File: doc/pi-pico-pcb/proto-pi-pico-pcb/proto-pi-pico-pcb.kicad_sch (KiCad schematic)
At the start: 13 parts

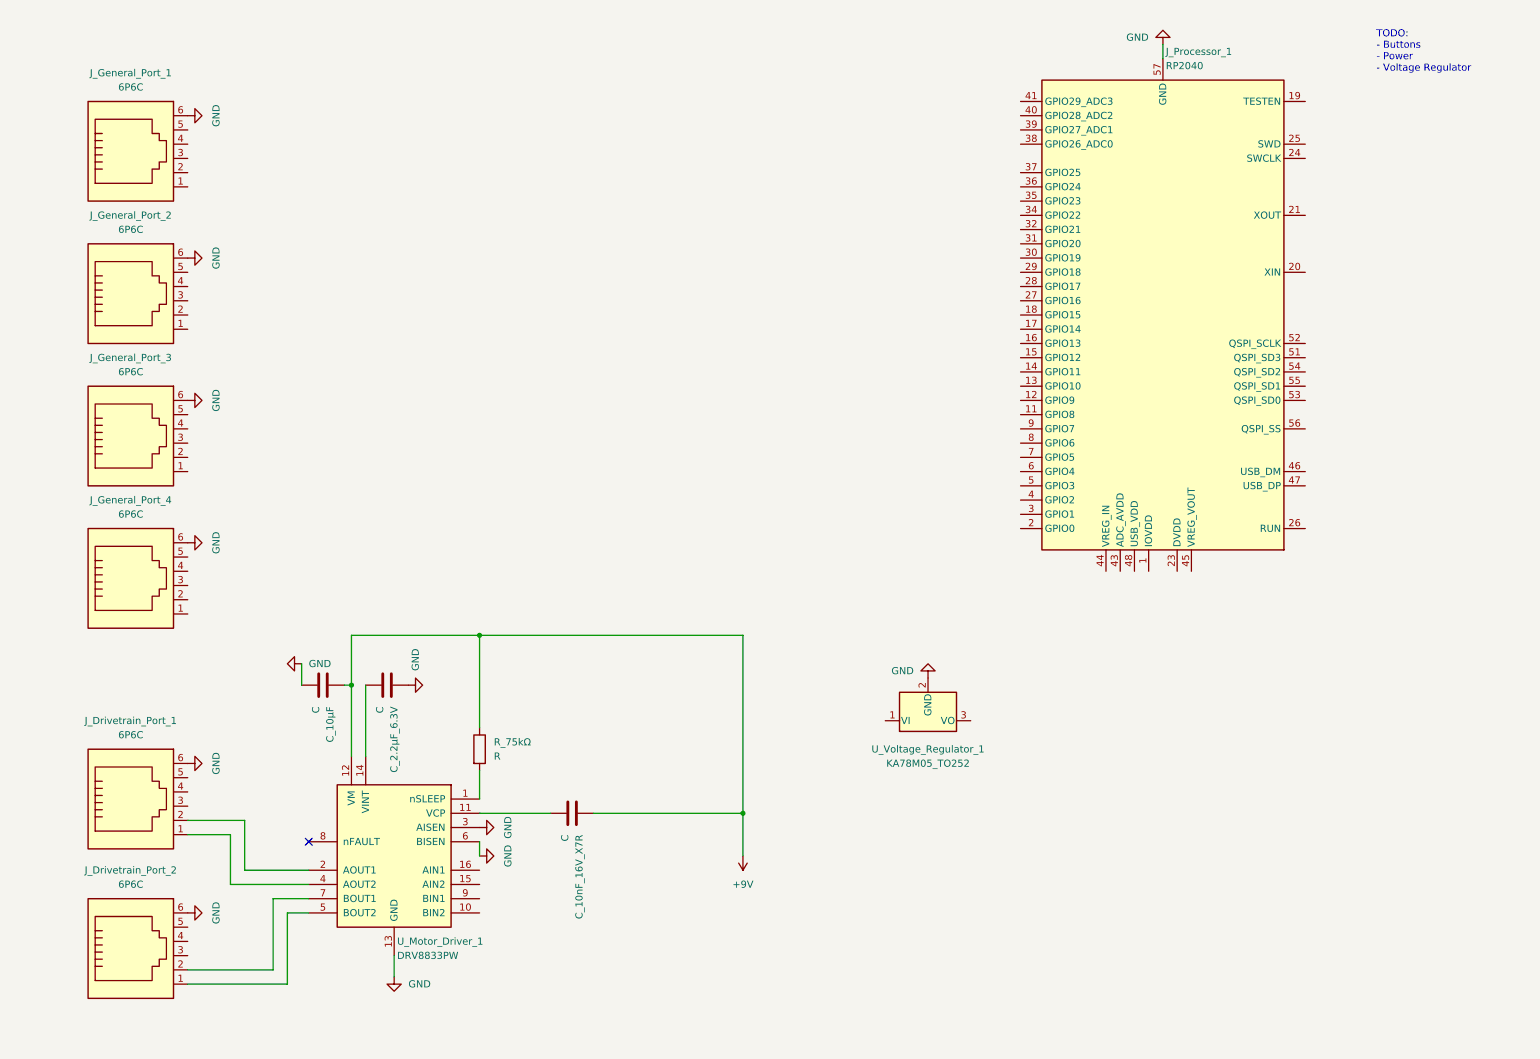
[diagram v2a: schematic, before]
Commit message: wired up external ports to bus
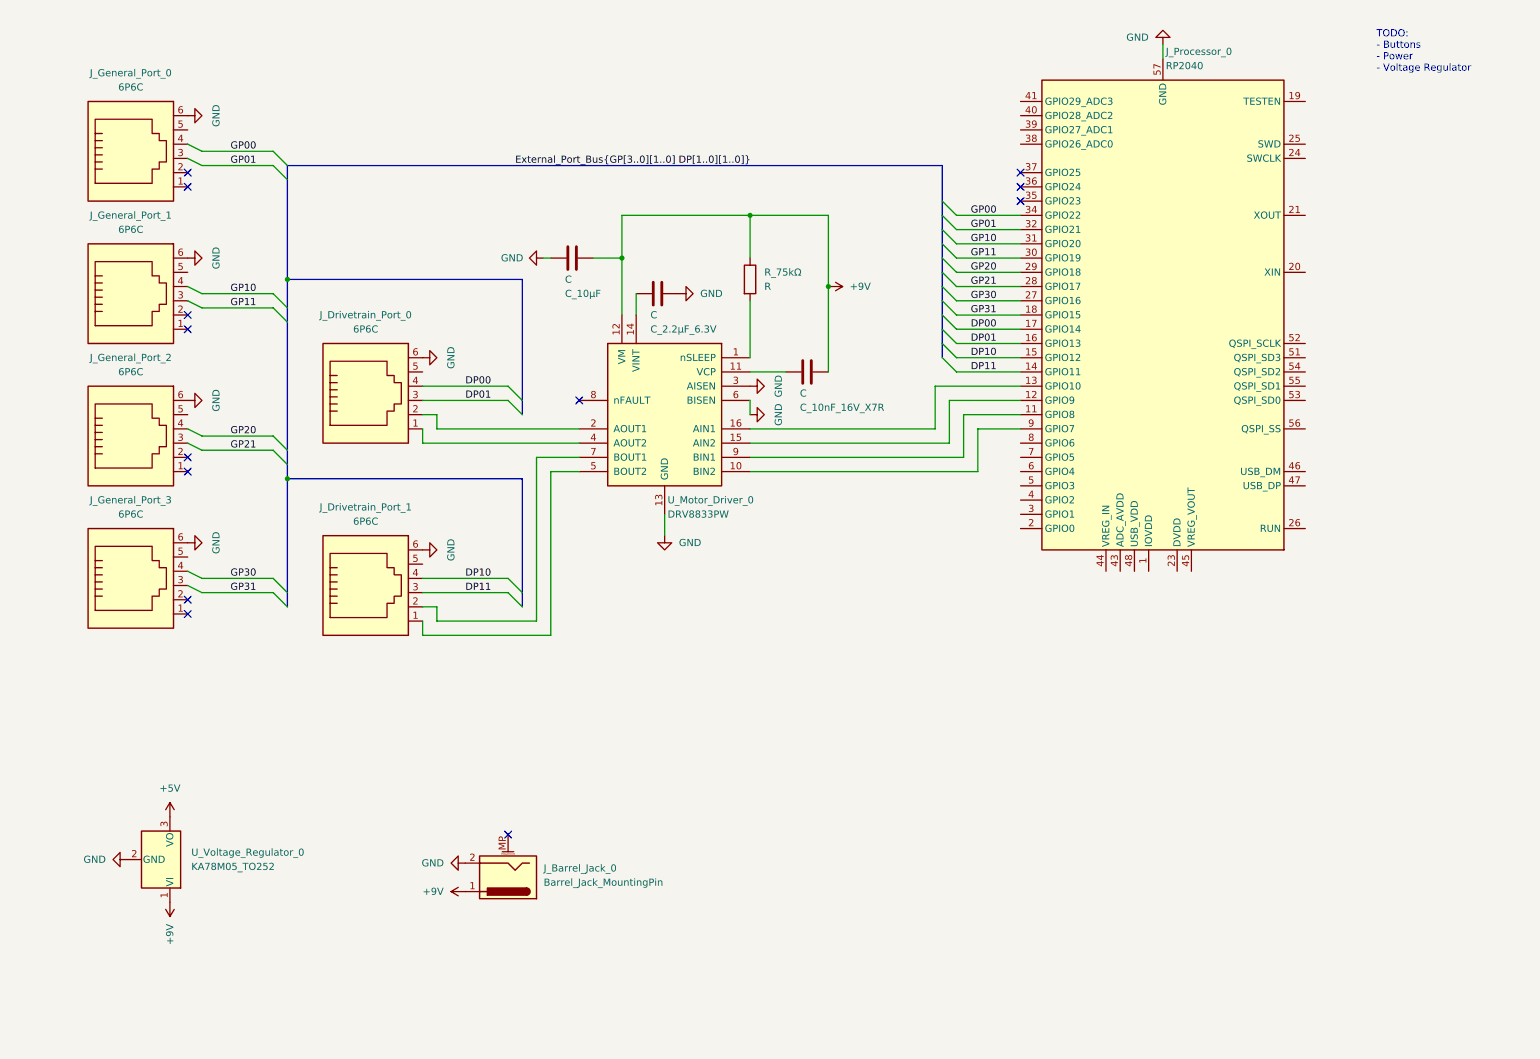
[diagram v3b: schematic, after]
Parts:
- added J_Barrel_Jack_0: Barrel_Jack_MountingPin, symbol Connector:Barrel_Jack_MountingPin
- renumbered J_Drivetrain_Port_1 to J_Drivetrain_Port_0, J_Drivetrain_Port_2 to J_Drivetrain_Port_1, J_General_Port_1 to J_General_Port_0, J_General_Port_2 to J_General_Port_1, J_General_Port_3 to J_General_Port_2, J_General_Port_4 to J_General_Port_3, J_Processor_1 to J_Processor_0, U_Motor_Driver_1 to U_Motor_Driver_0, U_Voltage_Regulator_1 to U_Voltage_Regulator_0
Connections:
- net +9V: now also U_Voltage_Regulator_0.1 (VI), J_Barrel_Jack_0.1
- net GND: now also J_Barrel_Jack_0.2
- net GP01: now reaches J_General_Port_0.3
- net GP01: now also J_Processor_0.32 (GPIO21)
- net GP00: now reaches J_General_Port_0.4
- net GP00: now also J_Processor_0.34 (GPIO22)
- net DP01: now reaches J_Drivetrain_Port_0.3
- net DP01: now also J_Processor_0.16 (GPIO13)
- net DP00: now reaches J_Drivetrain_Port_0.4
- net DP00: now also J_Processor_0.17 (GPIO14)
- net at J_Processor_0.11 (GPIO8): now also U_Motor_Driver_0.9 (BIN1)
- net at J_Processor_0.12 (GPIO9): now also U_Motor_Driver_0.15 (AIN2)
- net at J_Processor_0.13 (GPIO10): now also U_Motor_Driver_0.16 (AIN1)
- net DP11: now reaches J_Processor_0.14 (GPIO11)
- net DP11: now also J_Drivetrain_Port_1.3
- net DP10: now reaches J_Processor_0.15 (GPIO12)
- net DP10: now also J_Drivetrain_Port_1.4
- net GP31: now reaches J_Processor_0.18 (GPIO15)
- net GP31: now also J_General_Port_3.3
- net GP30: now reaches J_Processor_0.27 (GPIO16)
- net GP30: now also J_General_Port_3.4
- net GP21: now reaches J_Processor_0.28 (GPIO17)
- net GP21: now also J_General_Port_2.3
- net GP20: now reaches J_Processor_0.29 (GPIO18)
- net GP20: now also J_General_Port_2.4
- net GP11: now reaches J_Processor_0.30 (GPIO19)
- net GP11: now also J_General_Port_1.3
- net GP10: now reaches J_Processor_0.31 (GPIO20)
- net GP10: now also J_General_Port_1.4
- net at J_Processor_0.9 (GPIO7): now also U_Motor_Driver_0.10 (BIN2)
- net +5V: now reaches U_Voltage_Regulator_0.3 (VO)
- no-connect marks 1 -> 13
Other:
- moved on the sheet: C_10nF_16V_X7R, C_10μF, C_2.2μF_6.3V, J_Drivetrain_Port_0, J_Drivetrain_Port_1, R_75kΩ, U_Motor_Driver_0, U_Voltage_Regulator_0

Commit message: added general barrel jack
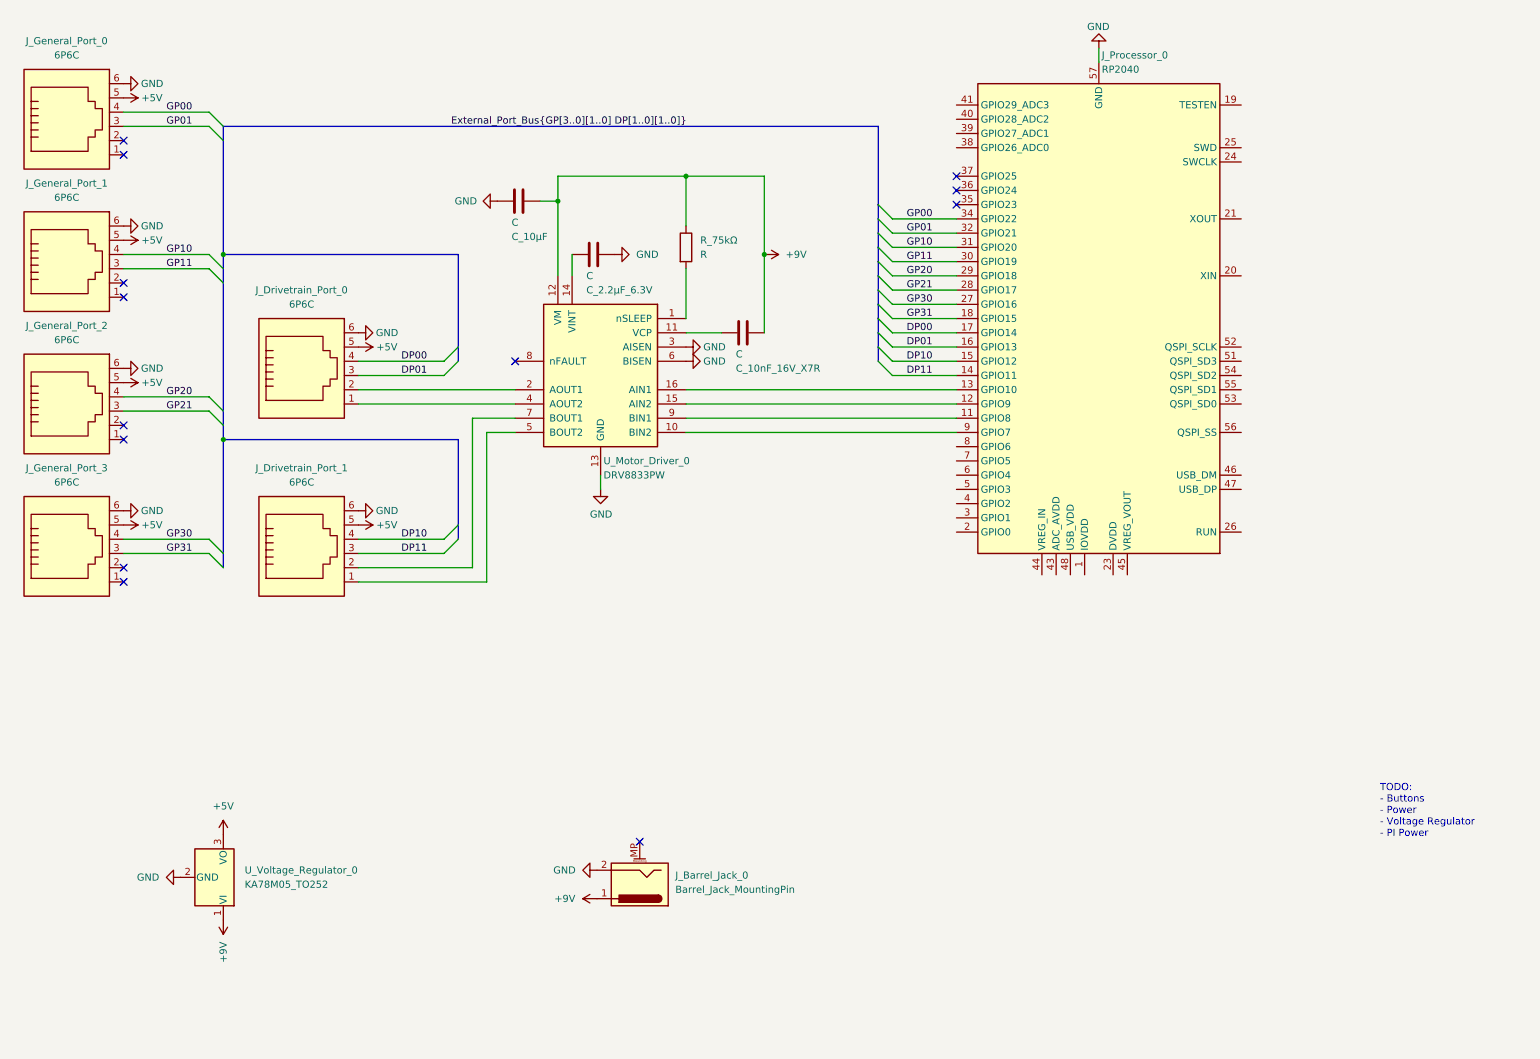
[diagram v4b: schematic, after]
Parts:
- J_Barrel_Jack_0: footprint (none) -> Connector_BarrelJack:BarrelJack_Horizontal
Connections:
- net +5V: now also J_Drivetrain_Port_0.5, J_Drivetrain_Port_1.5, J_General_Port_0.5, J_General_Port_1.5, J_General_Port_2.5, J_General_Port_3.5
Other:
- note added: "TODO: - Buttons - Power - Voltage Regulator - PI Power"
- note removed: "TODO: - Buttons - Power - Voltage Regulator"
- moved on the sheet: C_10nF_16V_X7R, C_10μF, C_2.2μF_6.3V, J_Barrel_Jack_0, J_Drivetrain_Port_0, J_Drivetrain_Port_1, J_General_Port_0, J_General_Port_1, J_General_Port_2, J_General_Port_3, J_Processor_0, R_75kΩ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

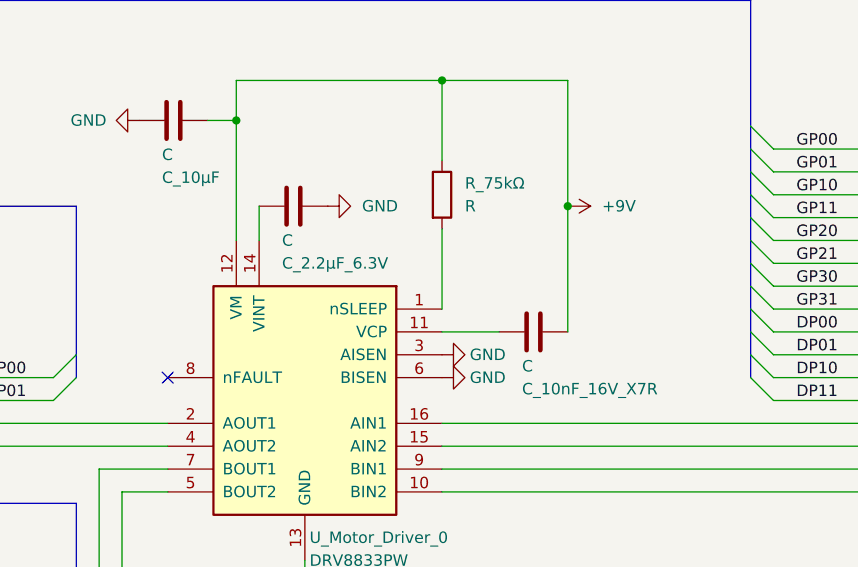
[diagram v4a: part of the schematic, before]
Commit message: gave general parts temporary footprints
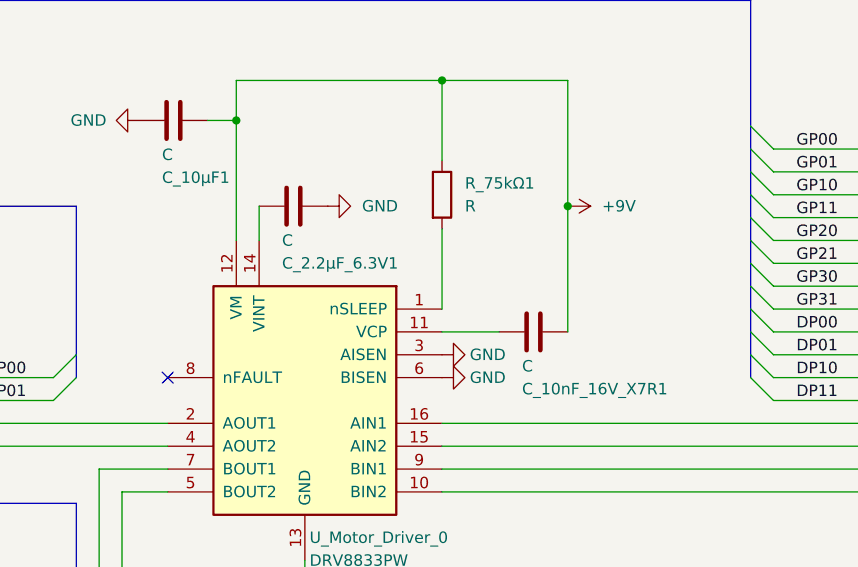
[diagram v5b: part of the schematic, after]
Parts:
- C_10nF_16V_X7R1: renamed from C_10nF_16V_X7R; footprint (none) -> Capacitor_SMD:CP_Elec_3x5.3
- C_10μF1: renamed from C_10μF; footprint (none) -> Capacitor_SMD:CP_Elec_3x5.3
- C_2.2μF_6.3V1: renamed from C_2.2μF_6.3V; footprint (none) -> Capacitor_SMD:CP_Elec_3x5.3
- J_Barrel_Jack_0: footprint Connector_BarrelJack:BarrelJack_Horizontal -> Connector_BarrelJack:BarrelJack_CUI_PJ-063AH_Horizontal
- J_Drivetrain_Port_0, J_Drivetrain_Port_1, J_General_Port_0, J_General_Port_1, J_General_Port_2, J_General_Port_3: footprint (none) -> Connector_RJ:RJ12_Amphenol_54601
- R_75kΩ1: renamed from R_75kΩ; footprint (none) -> Resistor_SMD:R_0201_0603Metric

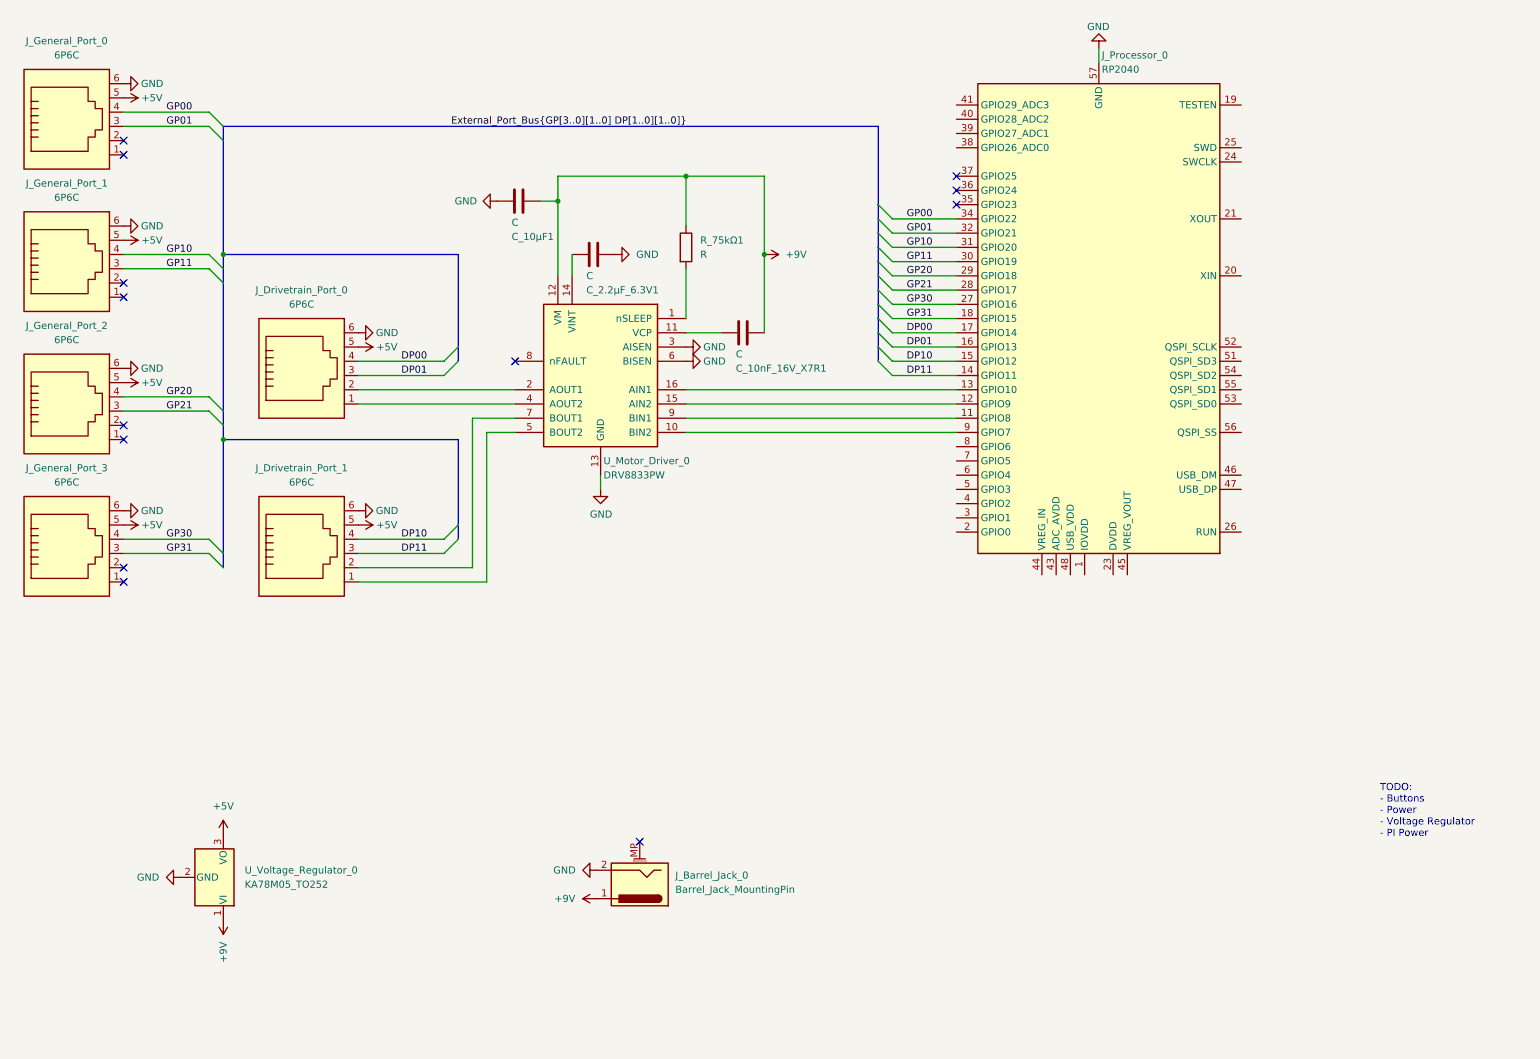
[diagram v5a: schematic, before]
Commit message: removed dead pins on rp2040
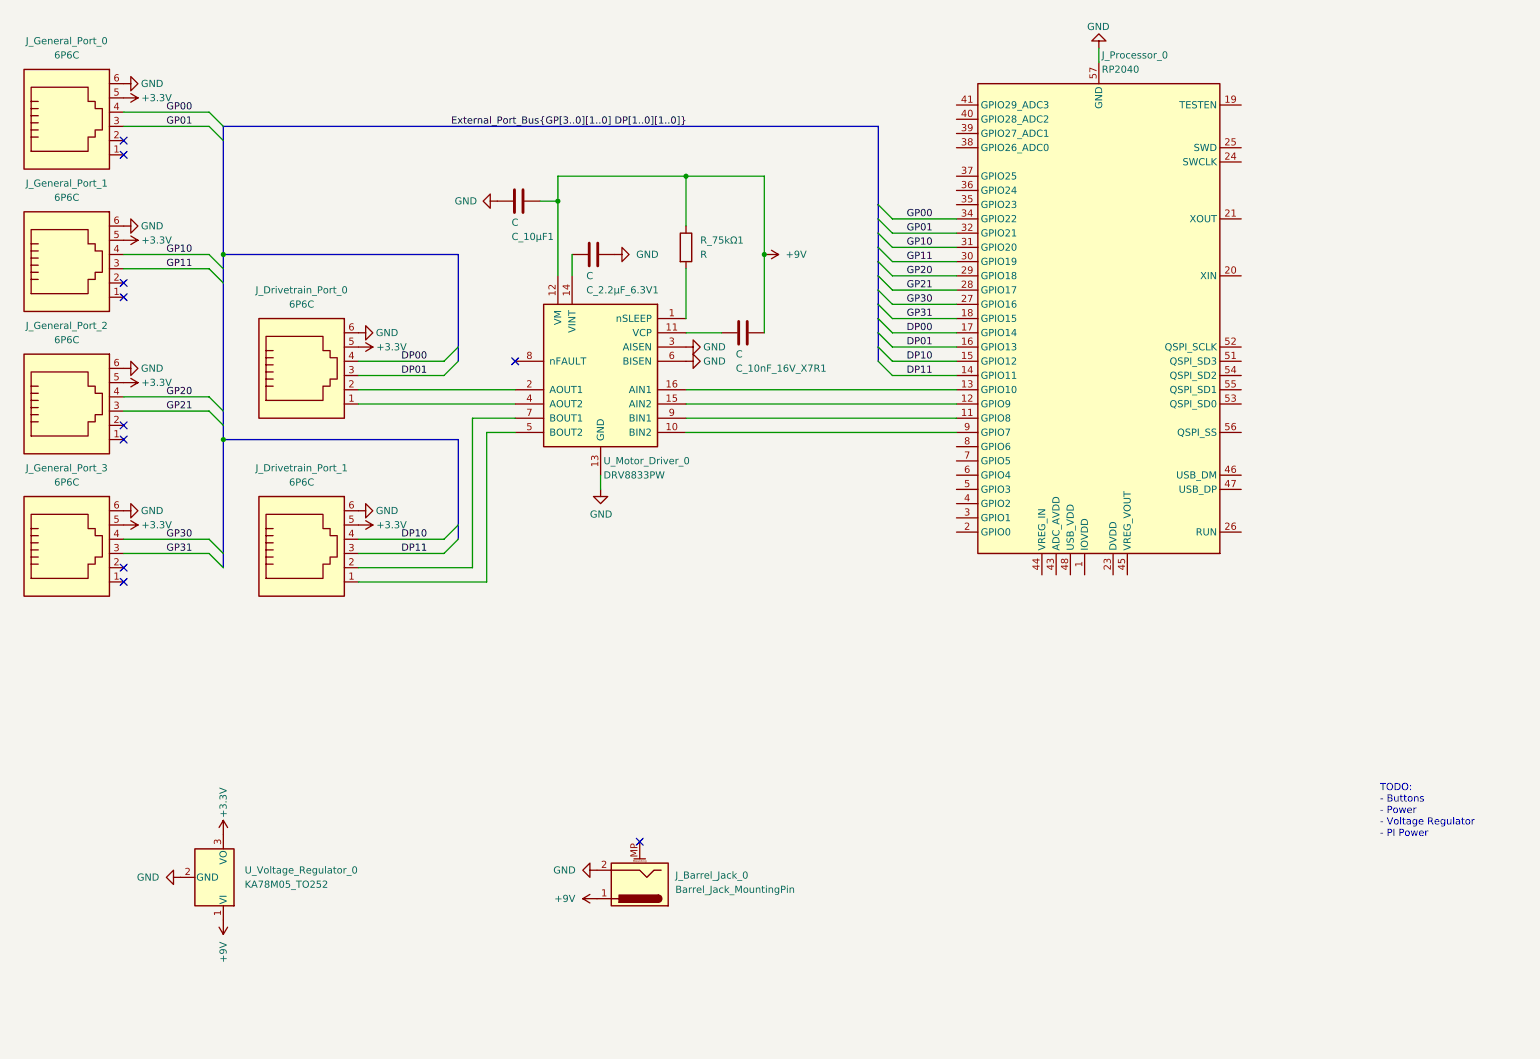
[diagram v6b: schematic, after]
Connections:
- net +5V renamed +3.3V
- no-connect marks 13 -> 10
